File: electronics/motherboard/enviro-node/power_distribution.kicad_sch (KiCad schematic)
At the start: 54 parts, among them J10 2604-3102, J7 2604-3102, J8 SOLAR_CRNT_JMPR, J9 BAT_CRNT_JMPR, U10 XC6215B332MR-G, U4 INA219BxD, U5 LT3652IMSE, U6 TPS22967DSGR, U7 MCP73832-2-OT, U8 INA219BxD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

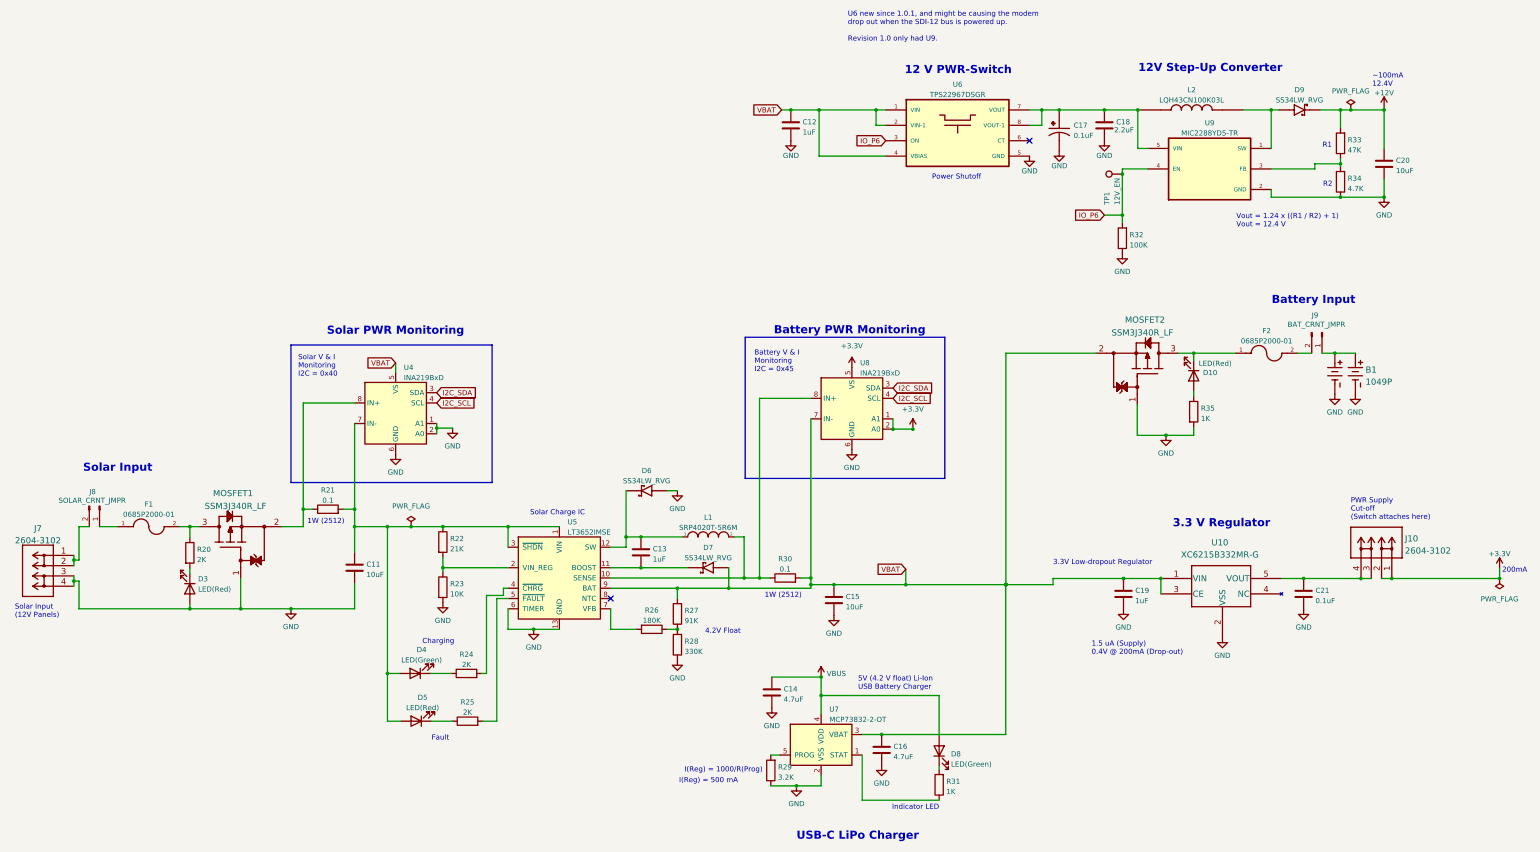
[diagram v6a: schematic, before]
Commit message: v1.0.3, added TMP1075 temp sensor, now using kicad 8.
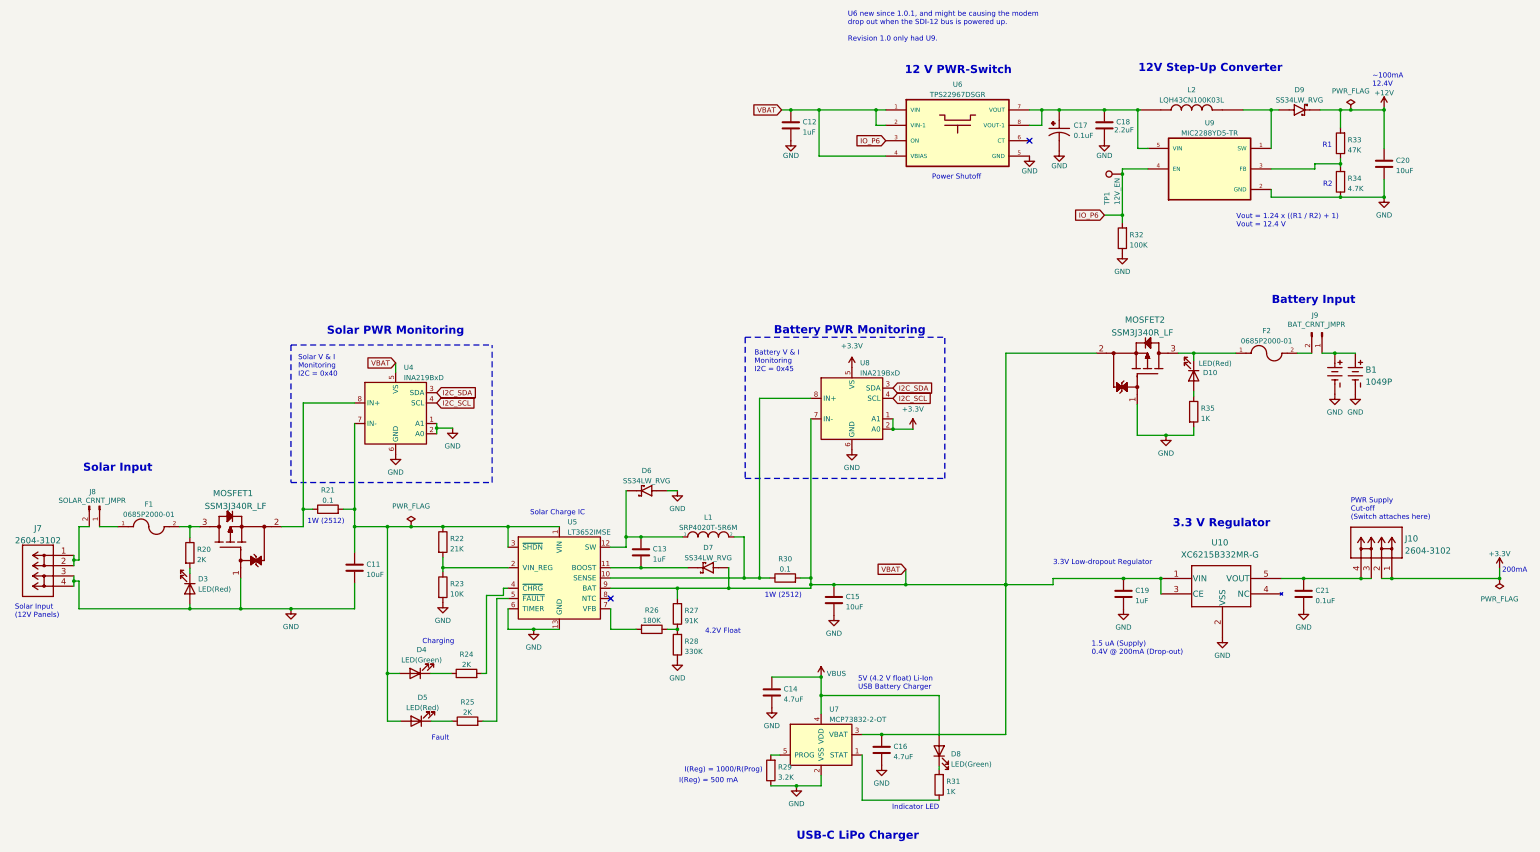
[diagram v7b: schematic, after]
